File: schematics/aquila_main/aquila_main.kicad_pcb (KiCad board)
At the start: 4 copper layers, 98 x 98 mm, 131 parts, among them IC1 MS5611-01BA03, J1 120591-1, J10 PYRO_3, J11 PYRO_2, J12 PYRO_4, J13 AudioJack3_SwitchTR, J14 SERVO, J2 1043P, J3 1043P, J4 PWR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

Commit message: preliminary placement of components
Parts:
- L1: value 150u -> 100u; footprint Inductor_THT:L_Toroid_Vertical_L24.6mm_W15.5mm_P11.44mm_Pulse_KM-4 -> aquila:L_MP0028_124_125_127
- L2: footprint Inductor_THT:L_Toroid_Vertical_L24.6mm_W15.5mm_P11.44mm_Pulse_KM-4 -> aquila:L_MP0028_124_125_127
- moved U6 356.4 mm to (194.0, 92.0), turned to -90 degrees
- moved U3 352.6 mm to (177.0, 94.0)
- moved D5 345.2 mm to (189.3, 118.0), turned to 180 degrees
- moved D6 343.9 mm to (190.0, 83.0), turned to 180 degrees
- moved R17 343.5 mm to (192.0, 108.0)
- moved J1 341.4 mm to (166.0, 115.0)
- moved R16 339.8 mm to (194.0, 87.0)
- moved R9 333.4 mm to (195.0, 98.0), turned to 90 degrees
- moved R5 331.9 mm to (186.0, 97.0), turned to 180 degrees
- moved R38 331.9 mm to (186.0, 91.0), turned to -90 degrees
- moved R28 329.1 mm to (168.0, 138.0), turned to 90 degrees
- moved J6 328.4 mm to (193.0, 76.0)
- moved D1 325.6 mm to (147.0, 75.0), turned to 90 degrees
- moved C10 323.0 mm to (160.0, 59.7), turned to 90 degrees
- moved R41 320.8 mm to (157.0, 136.0), turned to 90 degrees
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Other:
- board text added: "Origin: (150,100)"
- board text removed: "Origin wrt DXF plan: (150,110)"

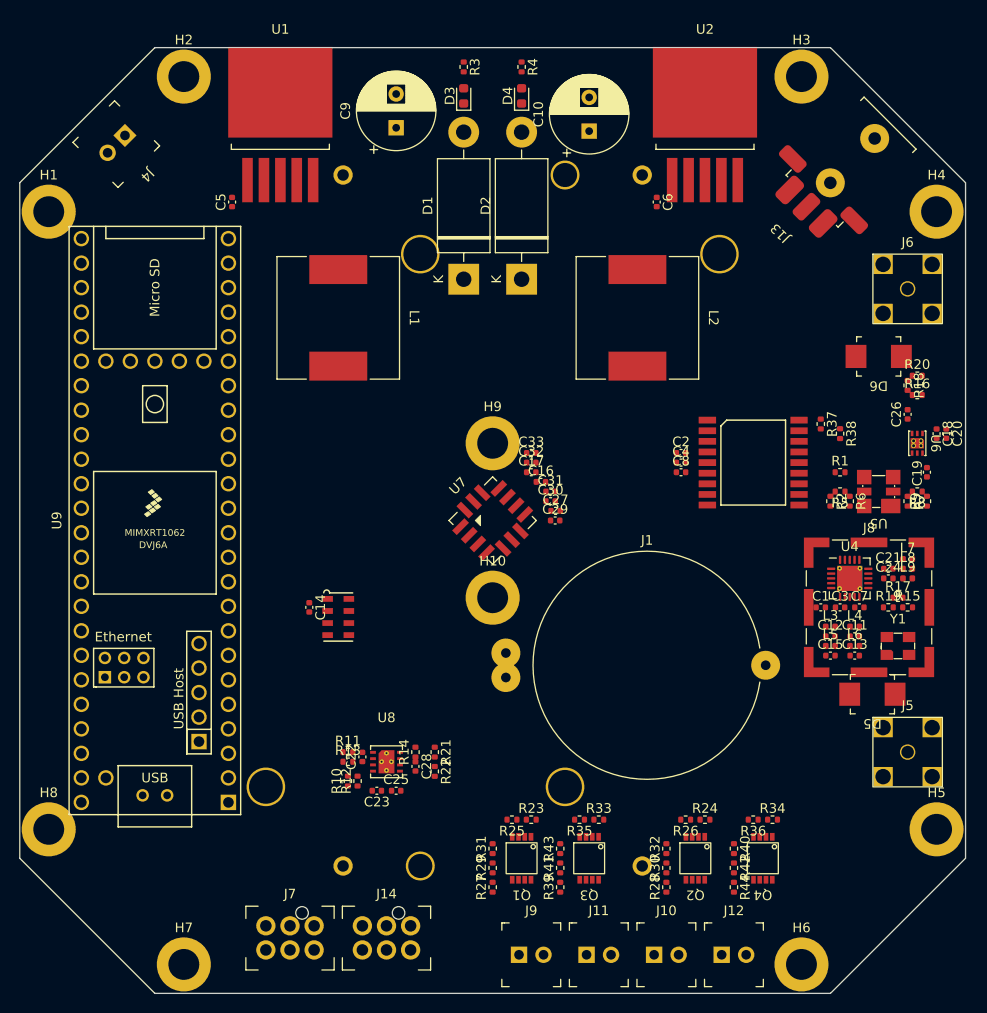
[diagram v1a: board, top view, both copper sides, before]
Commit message: placed all components and traces
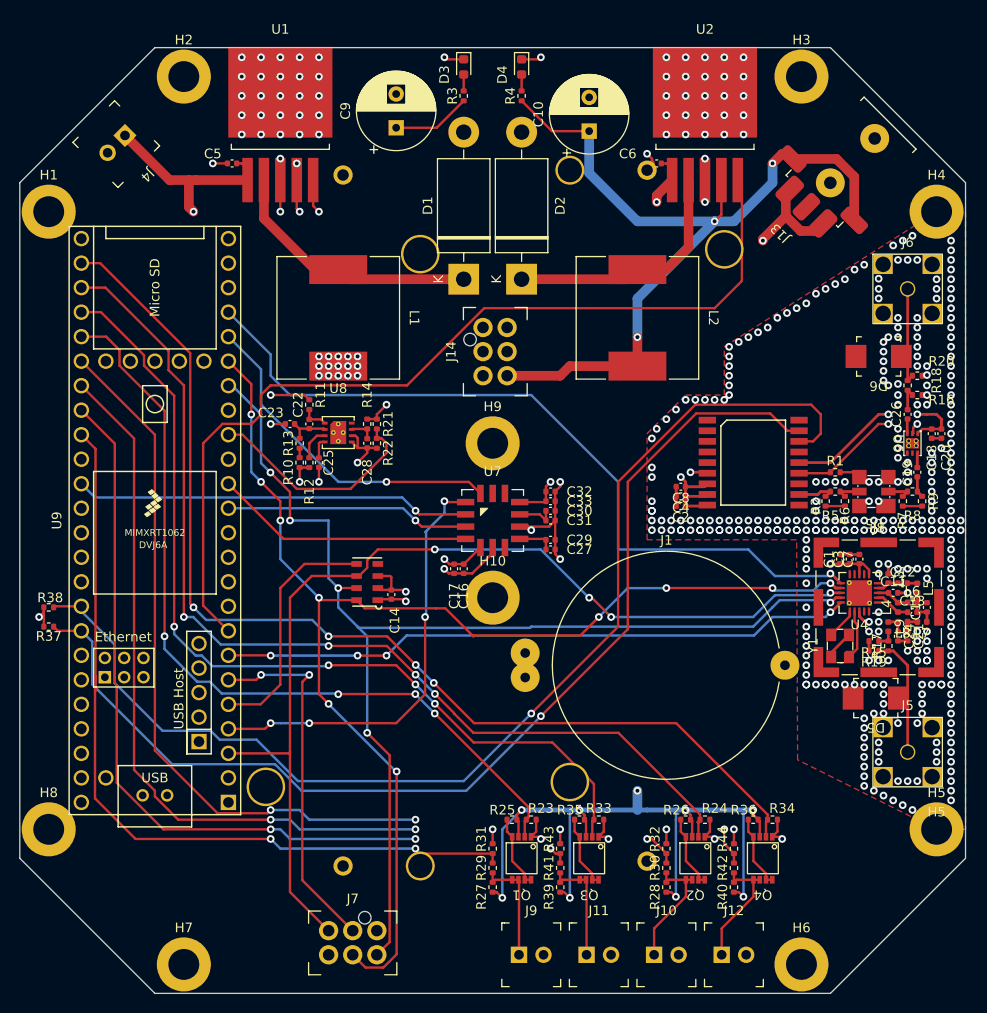
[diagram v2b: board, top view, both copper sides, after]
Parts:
- moved R38 84.0 mm to (104.0, 109.0), turned to 0 degrees
- moved R37 82.7 mm to (104.0, 111.0), turned to 0 degrees
- moved J14 60.3 mm to (149.0, 82.5), turned to 90 degrees
- moved C23 39.1 mm to (129.0, 90.0), turned to 0 degrees
- moved R11 36.2 mm to (131.0, 88.0), turned to -90 degrees
- moved C22 34.9 mm to (131.0, 90.0)
- moved C25 34.9 mm to (132.0, 94.0), turned to 90 degrees
- moved R21 34.5 mm to (138.0, 90.0)
- moved R22 34.5 mm to (138.0, 92.0)
- moved U8 34.5 mm to (134.0, 90.9)
- moved R14 34.4 mm to (137.0, 90.0)
- moved C28 33.9 mm to (137.0, 92.0)
- moved R10 33.4 mm to (130.0, 94.0)
- moved R12 33.4 mm to (131.0, 94.0)
- moved R13 33.4 mm to (130.0, 92.0), turned to 90 degrees
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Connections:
- L3 pad 1: 3v3 -> +3V3
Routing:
- net /pyro_pwr: track 0.00 -> 153.7 mm, vias 0 -> 10
- net /SCLK2: track 0.00 -> 132.8 mm, vias 0 -> 10
- net /MOSI2: track 0.00 -> 122.6 mm, vias 0 -> 5
- net /SDA: track 0.00 -> 119.6 mm, vias 0 -> 1
- net /SCL: track 0.00 -> 112.8 mm, vias 0 -> 1
- net /pyro_ch4: track 0.00 -> 112.4 mm, vias 0 -> 4
- net /pyro_cont4: track 0.00 -> 110.1 mm, vias 0 -> 3
- net /MISO2: track 0.00 -> 106.1 mm, vias 0 -> 4
- net /pyro_ch3: track 0.00 -> 104.4 mm, vias 0 -> 4
- net /pyro_cont3: track 0.00 -> 103.3 mm, vias 0 -> 3
- net /batt_p: track 0.00 -> 97.2 mm, vias 0 -> 3
- net /pyro_~{en}: track 0.00 -> 95.1 mm
- net /pyro_ch2: track 0.00 -> 94.1 mm, vias 0 -> 4
- net /pyro_cont2: track 0.00 -> 90.1 mm, vias 0 -> 3
- net Net-(J2-Pad1): track 0.00 -> 89.7 mm, vias 0 -> 1
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- added copper zone on In2.Cu, net +3V3
- added copper zone on F.Cu, net GND
- added copper zone on In1.Cu, net GND
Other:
- board text added: "H5"

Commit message: fixed relevant DRC errors
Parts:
- moved C6 2.24 mm to (166.0, 61.0), turned to 90 degrees
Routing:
- net GND: track 86.9 -> 97.1 mm, vias 394 -> 371
- net +3V3: track 44.1 -> 49.0 mm
- net /batt_p: track 97.2 -> 99.3 mm
- net /pyro_~{en}: track 95.1 -> 96.3 mm
- net /pyro_ch2: track 94.1 -> 94.8 mm
- added copper zone on B.Cu, net GND
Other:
- board text added: "EXT. BARO"
- board text added: "GPS"
- board text added: "PWR"
- board text added: "PYRO 1"
- board text added: "PYRO 2"
- board text added: "PYRO 3"
- board text added: "PYRO 4"
- board text added: "PYRO PWR"
- board text added: "PYRO SAFETY"
- board text added: "SERVO"
- board text added: "TELEM"
- board text removed: "H5"

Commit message: added silkscreen logo etc
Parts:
- added G***: LOGO, aquila:cusf_logo_full, F.Cu at (140.0, 119.0)
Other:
- board text added: "Aquila Flight Computer"
- board text added: "JLCJLCJLCJLC"

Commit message: minor adjustments
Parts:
- moved J3 0.20 mm to (134.3, 100.0)
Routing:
- net GND: track 97.1 -> 100.1 mm, vias 371 -> 372
- net +3V3: vias 24 -> 17
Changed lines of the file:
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@@
   )
   (footprint "aquila:1043" (layer "B.Cu")
-    (at 134.5 100 -90)
+    (at 134.3 100 -90)
     (property "DigiKey" "36-1043P-ND")
     (property "Sheetfile" "aquila_main.kicad_sch")
@@
   (via (at 169.5 95.5) (size 0.8) (drill 0.4) (layers "F.Cu" "B.Cu") (free) (net 1))
   (via (at 136 83) (size 0.8) (drill 0.4) (layers "F.Cu" "B.Cu") (net 1))
-  (via (at 132 84) (size 0.8) (drill 0.4) (layers "F.Cu" "B.Cu") (net 1))
-  (via (at 133 85) (size 0.8) (drill 0.4) (layers "F.Cu" "B.Cu") (net 1))
   (via (at 141 108.375) (size 0.8) (drill 0.4) (layers "F.Cu" "B.Cu") (net 1))
   (via (at 132 85) (size 0.8) (drill 0.4) (layers "F.Cu" "B.Cu") (net 1))
-  (via (at 133 83) (size 0.8) (drill 0.4) (layers "F.Cu" "B.Cu") (net 1))
-  (via (at 136 84) (size 0.8) (drill 0.4) (layers "F.Cu" "B.Cu") (net 1))
   (via (at 162.5 94) (size 0.8) (drill 0.4) (layers "F.Cu" "B.Cu") (net 1))
   (via (at 103 110) (size 0.8) (drill 0.4) (layers "F.Cu" "B.Cu") (net 1))
@@
   (via (at 191 104.5) (size 0.8) (drill 0.4) (layers "F.Cu" "B.Cu") (free) (net 1))
   (via (at 136 85) (size 0.8) (drill 0.4) (layers "F.Cu" "B.Cu") (net 1))
-  (via (at 135 85) (size 0.8) (drill 0.4) (layers "F.Cu" "B.Cu") (net 1))
   (via (at 134 83) (size 0.8) (drill 0.4) (layers "F.Cu" "B.Cu") (net 1))
   (via (at 134 85) (size 0.8) (drill 0.4) (layers "F.Cu" "B.Cu") (net 1))
   (via (at 135 84) (size 0.8) (drill 0.4) (layers "F.Cu" "B.Cu") (net 1))
   (via (at 185 104.5) (size 0.8) (drill 0.4) (layers "F.Cu" "B.Cu") (net 1))
-  (via (at 135 83) (size 0.8) (drill 0.4) (layers "F.Cu" "B.Cu") (net 1))
-  (via (at 134 84) (size 0.8) (drill 0.4) (layers "F.Cu" "B.Cu") (net 1))
   (via (at 145 104) (size 0.8) (drill 0.4) (layers "F.Cu" "B.Cu") (net 1))
   (via (at 156 96) (size 0.8) (drill 0.4) (layers "F.Cu" "B.Cu") (net 1))
@@
   (segment (start 139.5 107.195) (end 138.295 107.195) (width 0.25) (layer "F.Cu") (net 2))
   (segment (start 161.775 132.775) (end 162 133) (width 0.25) (layer "F.Cu") (net 2))
-  (segment (start 131.4 64.725) (end 131.4 67.4) (width 0.25) (layer "F.Cu") (net 2))
   (segment (start 166 60.52) (end 167.105 60.52) (width 0.25) (layer "F.Cu") (net 2))
   (segment (start 136.016 91.444) (end 136.016 92.48) (width 0.25) (layer "F.Cu") (net 2))
@@
   (segment (start 135.786 91.214) (end 136.016 91.444) (width 0.25) (layer "F.Cu") (net 2))
   (segment (start 179.51 131) (end 179.51 132.24) (width 0.25) (layer "F.Cu") (net 2))
+  (segment (start 172 68) (end 172 64.725) (width 0.25) (layer "F.Cu") (net 2))
   (segment (start 156.48 99) (end 156.48 98) (width 0.25) (layer "F.Cu") (net 2))
   (segment (start 156.48 97) (end 157 96.48) (width 0.25) (layer "F.Cu") (net 2))
@@
   (segment (start 137.97 92.48) (end 138 92.51) (width 0.25) (layer "F.Cu") (net 2))
   (segment (start 135.4 91.214) (end 134.325 91.214) (width 0.25) (layer "F.Cu") (net 2))
+  (segment (start 131.4 68) (end 131.4 64.725) (width 0.25) (layer "F.Cu") (net 2))
   (segment (start 167.105 60.52) (end 172 55.625) (width 0.25) (layer "F.Cu") (net 2))
   (segment (start 150 103.36) (end 150 102.8) (width 0.25) (layer "F.Cu") (net 2))
@@
   (segment (start 147 52.2125) (end 145.2125 52.2125) (width 0.25) (layer "F.Cu") (net 2))
   (segment (start 186 103.52) (end 187 103.52) (width 0.25) (layer "F.Cu") (net 2))
-  (segment (start 131.4 67.4) (end 132 68) (width 0.25) (layer "F.Cu") (net 2))
   (segment (start 156.48 100) (end 156.48 102) (width 0.25) (layer "F.Cu") (net 2))
   (segment (start 145.455402 105.48) (end 144.987701 105.012299) (width 0.25) (layer "F.Cu") (net 2))
@@
   (via (at 186.5 100) (size 0.8) (drill 0.4) (layers "F.Cu" "B.Cu") (free) (net 2))
   (via (at 197.5 109) (size 0.8) (drill 0.4) (layers "F.Cu" "B.Cu") (free) (net 2))
-  (via (at 172 62.5) (size 0.8) (drill 0.4) (layers "F.Cu" "B.Cu") (net 2))
+  (via (at 172 63) (size 0.8) (drill 0.4) (layers "F.Cu" "B.Cu") (net 2))
   (via (at 195 88) (size 0.8) (drill 0.4) (layers "F.Cu" "B.Cu") (free) (net 2))
   (via (at 128 52) (size 0.8) (drill 0.4) (layers "F.Cu" "B.Cu") (net 2))
@@
   (via (at 197.5 114) (size 0.8) (drill 0.4) (layers "F.Cu" "B.Cu") (free) (net 2))
   (via (at 195.5 98) (size 0.8) (drill 0.4) (layers "F.Cu" "B.Cu") (free) (net 2))
-  (via (at 172 67) (size 0.8) (drill 0.4) (layers "F.Cu" "B.Cu") (net 2))
+  (via (at 172 68) (size 0.8) (drill 0.4) (layers "F.Cu" "B.Cu") (net 2))
   (via (at 128 54) (size 0.8) (drill 0.4) (layers "F.Cu" "B.Cu") (net 2))
   (via (at 194.5 118) (size 0.8) (drill 0.4) (layers "F.Cu" "B.Cu") (free) (net 2))
@@
   (via (at 192 96) (size 0.8) (drill 0.4) (layers "F.Cu" "B.Cu") (free) (net 2))
   (via (at 190 76) (size 0.8) (drill 0.4) (layers "F.Cu" "B.Cu") (free) (net 2))
+  (via (at 131.4 63) (size 0.8) (drill 0.4) (layers "F.Cu" "B.Cu") (net 2))
   (via (at 124 52) (size 0.8) (drill 0.4) (layers "F.Cu" "B.Cu") (net 2))
   (via (at 194.2 83) (size 0.8) (drill 0.4) (layers "F.Cu" "B.Cu") (free) (net 2))
@@
   (via (at 193 73) (size 0.8) (drill 0.4) (layers "F.Cu" "B.Cu") (free) (net 2))
   (via (at 130 58) (size 0.8) (drill 0.4) (layers "F.Cu" "B.Cu") (net 2))
-  (via (at 132 68) (size 0.8) (drill 0.4) (layers "F.Cu" "B.Cu") (net 2))
+  (via (at 131.4 68) (size 0.8) (drill 0.4) (layers "F.Cu" "B.Cu") (net 2))
   (via (at 188.5 122.5) (size 0.8) (drill 0.4) (layers "F.Cu" "B.Cu") (free) (net 2))
   (via (at 174.5 100) (size 0.8) (drill 0.4) (layers "F.Cu" "B.Cu") (free) (net 2))
